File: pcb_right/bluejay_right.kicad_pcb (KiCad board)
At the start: 2 copper layers, 0 parts

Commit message: Begin work on right pcb
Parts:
- added C6: 4.7u, BlueJay footprints:CP_Radial_D4.0mm_P1.50mm, F.Cu at (80.6, 42.8)
- added C7: 100n, BlueJay footprints:C_Disc_D4.3mm_W1.9mm_P5.00mm, F.Cu at (82.0, 87.2)
- added Da1: 1N4148, BlueJay footprints:D_DO-35_SOD27_P5.08mm_Horizontal, F.Cu at (40.7, 127.8)
- added Da2: 1N4148, BlueJay footprints:D_DO-35_SOD27_P5.08mm_Horizontal, F.Cu at (41.2, 134.2)
- added Da3: 1N4148, BlueJay footprints:D_DO-35_SOD27_P5.08mm_Horizontal, F.Cu at (40.9, 139.2)
- added Da4: 1N4148, BlueJay footprints:D_DO-35_SOD27_P5.08mm_Horizontal, F.Cu at (40.4, 145.5)
- added Da5: 1N4148, BlueJay footprints:D_DO-35_SOD27_P5.08mm_Horizontal, F.Cu at (39.7, 152.2)
- added Db1: 1N4148, BlueJay footprints:D_DO-35_SOD27_P5.08mm_Horizontal, F.Cu at (51.9, 128.0)
- added Db2: 1N4148, BlueJay footprints:D_DO-35_SOD27_P5.08mm_Horizontal, F.Cu at (51.7, 133.8)
- added Db3: 1N4148, BlueJay footprints:D_DO-35_SOD27_P5.08mm_Horizontal, F.Cu at (51.7, 138.8)
- added Db4: 1N4148, BlueJay footprints:D_DO-35_SOD27_P5.08mm_Horizontal, F.Cu at (51.9, 145.0)
- added Db5: 1N4148, BlueJay footprints:D_DO-35_SOD27_P5.08mm_Horizontal, F.Cu at (51.7, 152.2)
- added Dc1: 1N4148, BlueJay footprints:D_DO-35_SOD27_P5.08mm_Horizontal, F.Cu at (61.2, 128.0)
- added Dc2: 1N4148, BlueJay footprints:D_DO-35_SOD27_P5.08mm_Horizontal, F.Cu at (61.2, 133.5)
- added Dc3: 1N4148, BlueJay footprints:D_DO-35_SOD27_P5.08mm_Horizontal, F.Cu at (60.9, 138.0)
- added Dc4: 1N4148, BlueJay footprints:D_DO-35_SOD27_P5.08mm_Horizontal, F.Cu at (61.4, 144.5)
- added Dc5: 1N4148, BlueJay footprints:D_DO-35_SOD27_P5.08mm_Horizontal, F.Cu at (61.9, 151.5)
- added Dd1: 1N4148, BlueJay footprints:D_DO-35_SOD27_P5.08mm_Horizontal, F.Cu at (202.2, 11.2)
- added Dd2: 1N4148, BlueJay footprints:D_DO-35_SOD27_P5.08mm_Horizontal, F.Cu at (202.7, 16.2)
- added Dd3: 1N4148, BlueJay footprints:D_DO-35_SOD27_P5.08mm_Horizontal, F.Cu at (202.4, 21.2)
- added Dd4: 1N4148, BlueJay footprints:D_DO-35_SOD27_P5.08mm_Horizontal, F.Cu at (202.4, 25.2)
- added Dd5: 1N4148, BlueJay footprints:D_DO-35_SOD27_P5.08mm_Horizontal, F.Cu at (166.4, 127.5)
- added De1: 1N4148, BlueJay footprints:D_DO-35_SOD27_P5.08mm_Horizontal, F.Cu at (213.2, 11.2)
- added De2: 1N4148, BlueJay footprints:D_DO-35_SOD27_P5.08mm_Horizontal, F.Cu at (213.2, 25.0)
- added De3: 1N4148, BlueJay footprints:D_DO-35_SOD27_P5.08mm_Horizontal, F.Cu at (212.9, 17.5)
- added De4: 1N4148, BlueJay footprints:D_DO-35_SOD27_P5.08mm_Horizontal, F.Cu at (213.2, 21.2)
- added Df2: 1N4148, BlueJay footprints:D_DO-35_SOD27_P5.08mm_Horizontal, F.Cu at (227.9, 47.2)
- added Df3: 1N4148, BlueJay footprints:D_DO-35_SOD27_P5.08mm_Horizontal, F.Cu at (227.7, 51.2)
- added Df4: 1N4148, BlueJay footprints:D_DO-35_SOD27_P5.08mm_Horizontal, F.Cu at (227.9, 55.0)
- added J2: SJ-43514, BlueJay footprints:CUI_SJ-43514, F.Cu at (86.1, 32.5)
- added R5: 2.2k, BlueJay footprints:R_Axial_DIN0204_L3.6mm_D1.6mm_P5.08mm_Horizontal, F.Cu at (85.7, 43.1)
- added R6: 2.2k, BlueJay footprints:R_Axial_DIN0204_L3.6mm_D1.6mm_P5.08mm_Horizontal, F.Cu at (78.6, 37.3)
- added SWa1: KEYSW, BlueJay footprints:SW_MX, F.Cu at (116.7, 47.6)
- added SWa2: KEYSW, BlueJay footprints:SW_MX, F.Cu at (116.7, 66.7)
- added SWa3: KEYSW, BlueJay footprints:SW_MX, F.Cu at (116.7, 85.7)
- added SWa4: KEYSW, BlueJay footprints:SW_MX, F.Cu at (116.7, 104.8)
- added SWa5: KEYSW, BlueJay footprints:SW_MX, F.Cu at (87.5, 152.9)
- added SWb1: KEYSW, BlueJay footprints:SW_MX, F.Cu at (135.7, 45.2)
- added SWb2: KEYSW, BlueJay footprints:SW_MX, F.Cu at (135.7, 64.3)
- added SWb3: KEYSW, BlueJay footprints:SW_MX, F.Cu at (135.7, 83.3)
- added SWb4: KEYSW, BlueJay footprints:SW_MX, F.Cu at (135.7, 102.4)
- added SWb5: KEYSW, BlueJay footprints:SW_MX, F.Cu at (104.8, 140.5)
- added SWc1: KEYSW, BlueJay footprints:SW_MX, F.Cu at (154.8, 38.1)
- added SWc2: KEYSW, BlueJay footprints:SW_MX, F.Cu at (154.8, 57.1)
- added SWc3: KEYSW, BlueJay footprints:SW_MX, F.Cu at (154.8, 76.2)
- added SWc4: KEYSW, BlueJay footprints:SW_MX, F.Cu at (154.8, 95.2)
- added SWc5: KEYSW, BlueJay footprints:SW_MX, F.Cu at (123.8, 133.3)
- added SWd1: KEYSW, BlueJay footprints:SW_MX, F.Cu at (173.8, 45.2)
- added SWd2: KEYSW, BlueJay footprints:SW_MX, F.Cu at (173.8, 64.3)
- added SWd3: KEYSW, BlueJay footprints:SW_MX, F.Cu at (173.8, 83.3)
- added SWd4: KEYSW, BlueJay footprints:SW_MX, F.Cu at (173.8, 102.4)
- added SWd5: KEYSW, BlueJay footprints:SW_MX, F.Cu at (145.3, 128.6)
- added SWe1: KEYSW, BlueJay footprints:SW_MX, F.Cu at (192.9, 52.4)
- added SWe2: KEYSW, BlueJay footprints:SW_MX, F.Cu at (192.9, 71.4)
- added SWe3: KEYSW, BlueJay footprints:SW_MX, F.Cu at (192.9, 90.5)
- added SWe4: KEYSW, BlueJay footprints:SW_MX, F.Cu at (192.9, 109.5)
- added SWf2: KEYSW, BlueJay footprints:SW_MX, F.Cu at (211.9, 71.4)
- added SWf3: KEYSW, BlueJay footprints:SW_MX, F.Cu at (211.9, 90.5)
- added SWf4: KEYSW, BlueJay footprints:SW_MX, F.Cu at (211.9, 109.5)
- added U2: MCP23017, Package_DIP_AKL:DIP-28_W7.62mm_Socket, F.Cu at (84.9, 68.1)
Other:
- board outline added: 147 x 140.5 mm

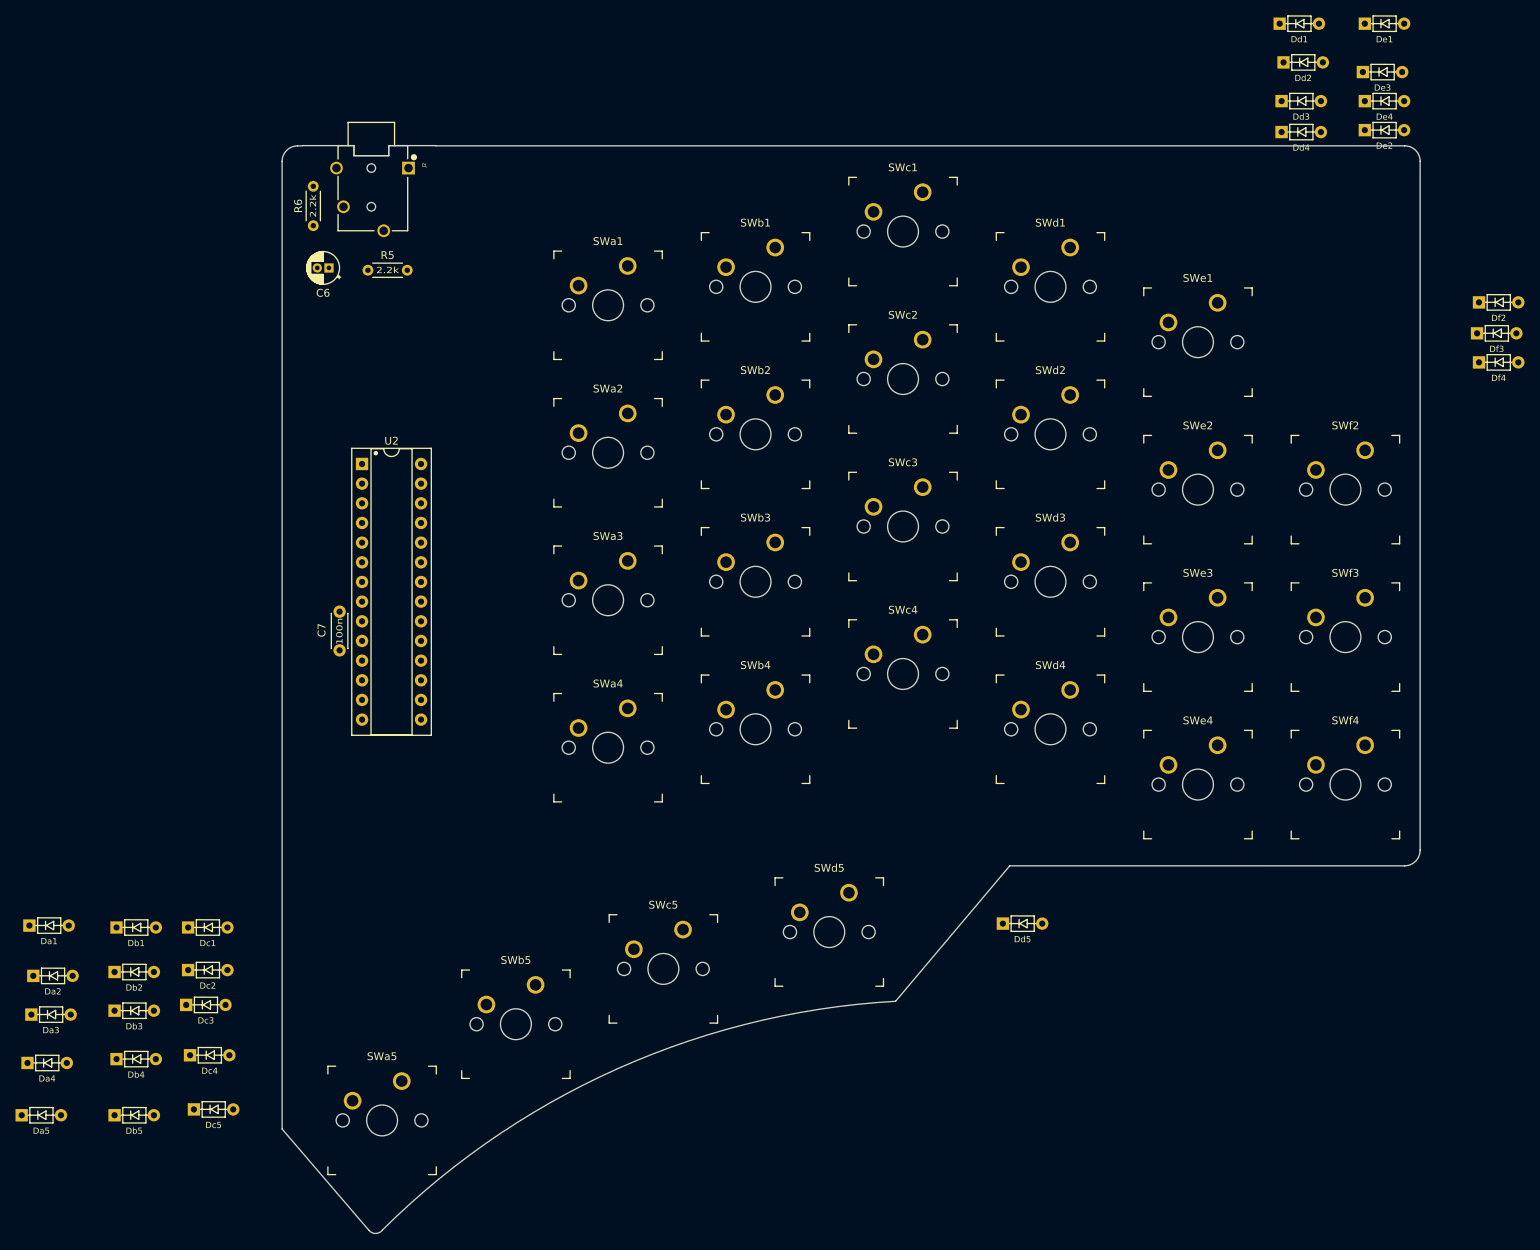
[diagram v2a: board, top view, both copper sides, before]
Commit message: Routing of right PCB
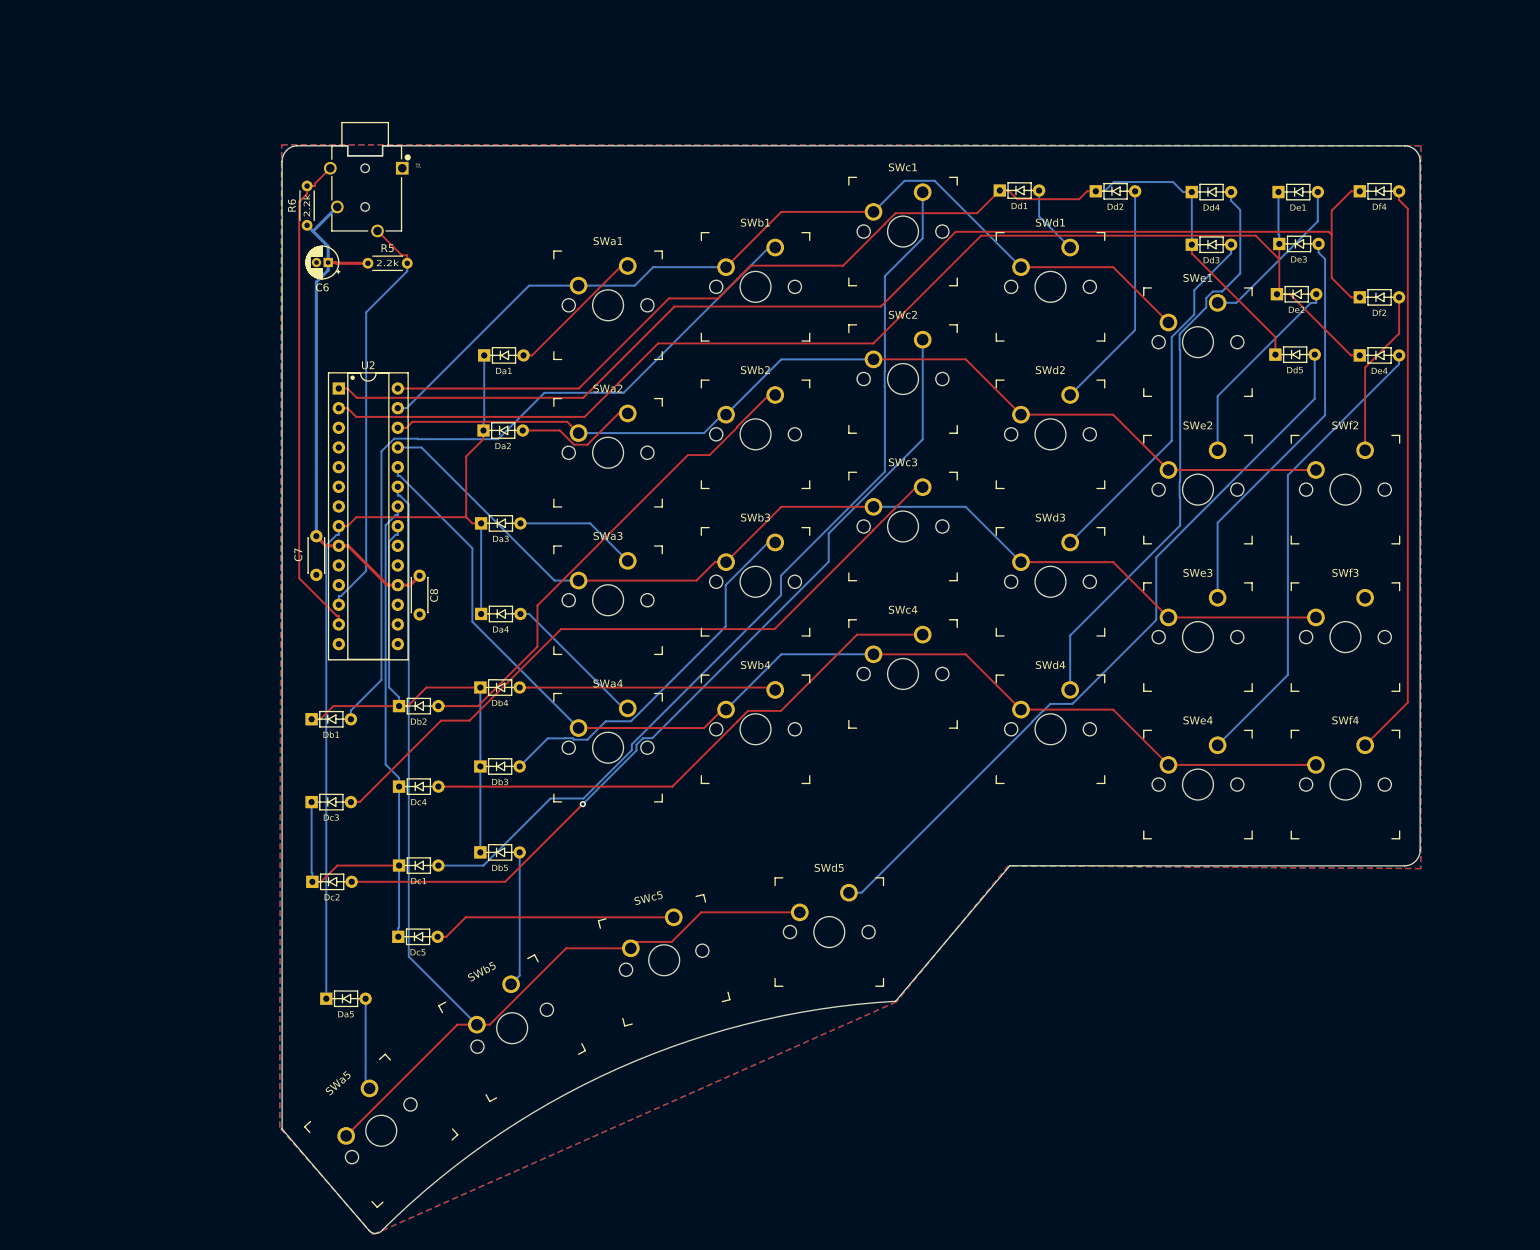
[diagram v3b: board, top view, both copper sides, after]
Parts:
- removed Df3: 1N4148, BlueJay footprints:D_DO-35_SOD27_P5.08mm_Horizontal
- added C8: 100n, BlueJay footprints:C_Disc_D4.3mm_W1.9mm_P5.00mm, F.Cu at (92.3, 82.6)
- moved Da1 94.2 mm to (99.4, 54.1)
- moved Da2 91.3 mm to (99.3, 63.8)
- moved Da3 86.0 mm to (99.0, 75.8)
- moved Da4 82.4 mm to (99.0, 87.5)
- moved Dd5 81.5 mm to (201.6, 54.0)
- moved Db4 67.2 mm to (98.9, 97.0)
- moved Db5 58.2 mm to (98.9, 118.3)
- moved Db3 56.8 mm to (98.9, 107.2)
- moved Db2 50.3 mm to (88.4, 99.4)
- moved Dc4 44.0 mm to (88.4, 109.8)
- moved Da5 42.1 mm to (79.0, 137.2)
- moved Dd1 42.1 mm to (166.0, 32.8)
- moved Db1 36.9 mm to (77.1, 101.1)
- moved Dc5 34.6 mm to (88.3, 129.2)
- moved De4 32.9 mm to (212.5, 54.1)
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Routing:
- net /colE: track 0.00 -> 160.1 mm
- net /colF: track 0.00 -> 155.8 mm
- net /row4: track 0.00 -> 148.7 mm
- net /row5: track 0.00 -> 144.4 mm
- net /colD: track 0.00 -> 140.6 mm
- net /row3: track 0.00 -> 135.6 mm
- net /row2: track 0.00 -> 129.4 mm
- net /row1: track 0.00 -> 119.3 mm
- net Net-(Dc1-Pad2): track 0.00 -> 118.8 mm
- net /colA: track 0.00 -> 114.6 mm
- net Net-(Dc2-Pad2): track 0.00 -> 112.9 mm, vias 0 -> 1
- net Net-(Db1-Pad2): track 0.00 -> 98.1 mm
- net Net-(Dd5-Pad2): track 0.00 -> 97.1 mm
- net Net-(Dc3-Pad2): track 0.00 -> 90.7 mm
- net /colC: track 0.00 -> 79.6 mm
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- added copper zone on B.Cu, net GND
- added copper zone on F.Cu, net GND
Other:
- outline, holes or cut-outs redrawn

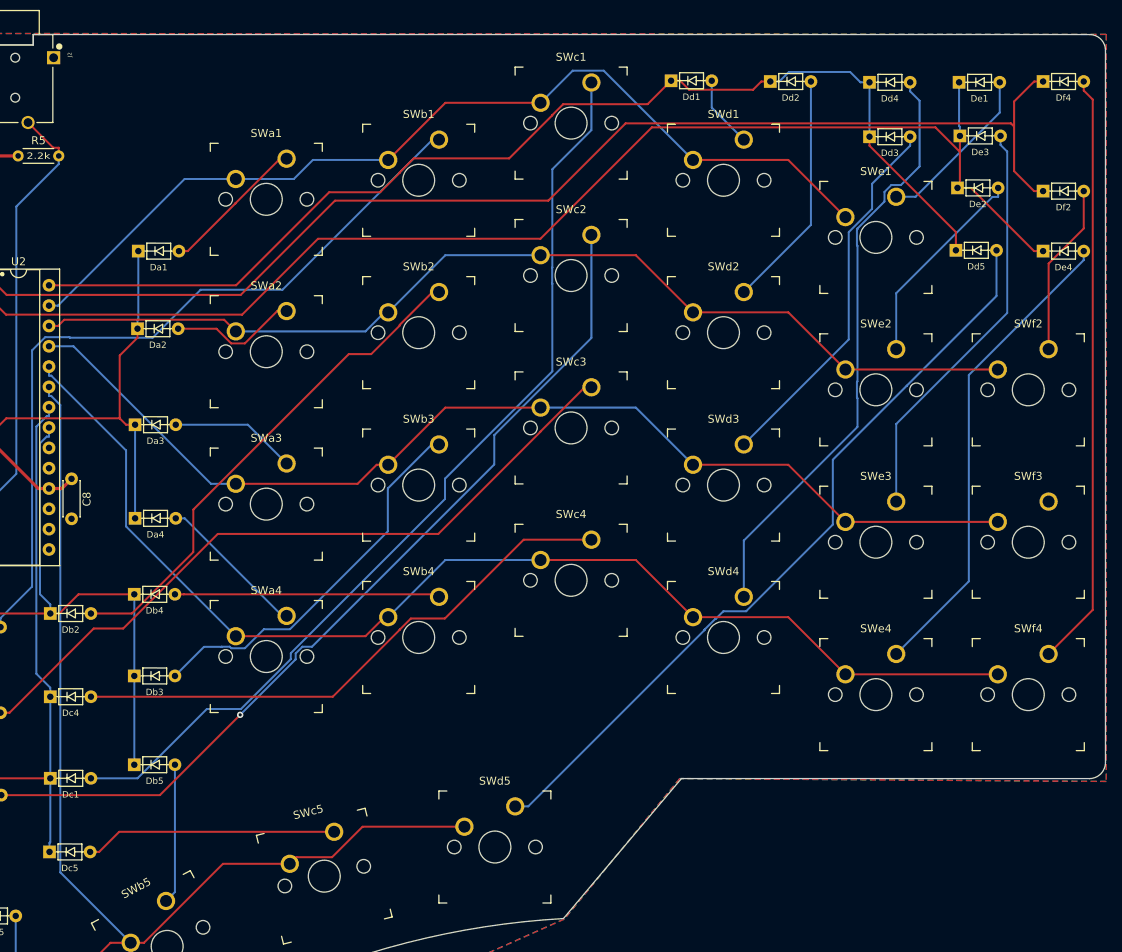
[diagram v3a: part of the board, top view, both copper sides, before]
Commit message: Fine tune placement of switches - right hand
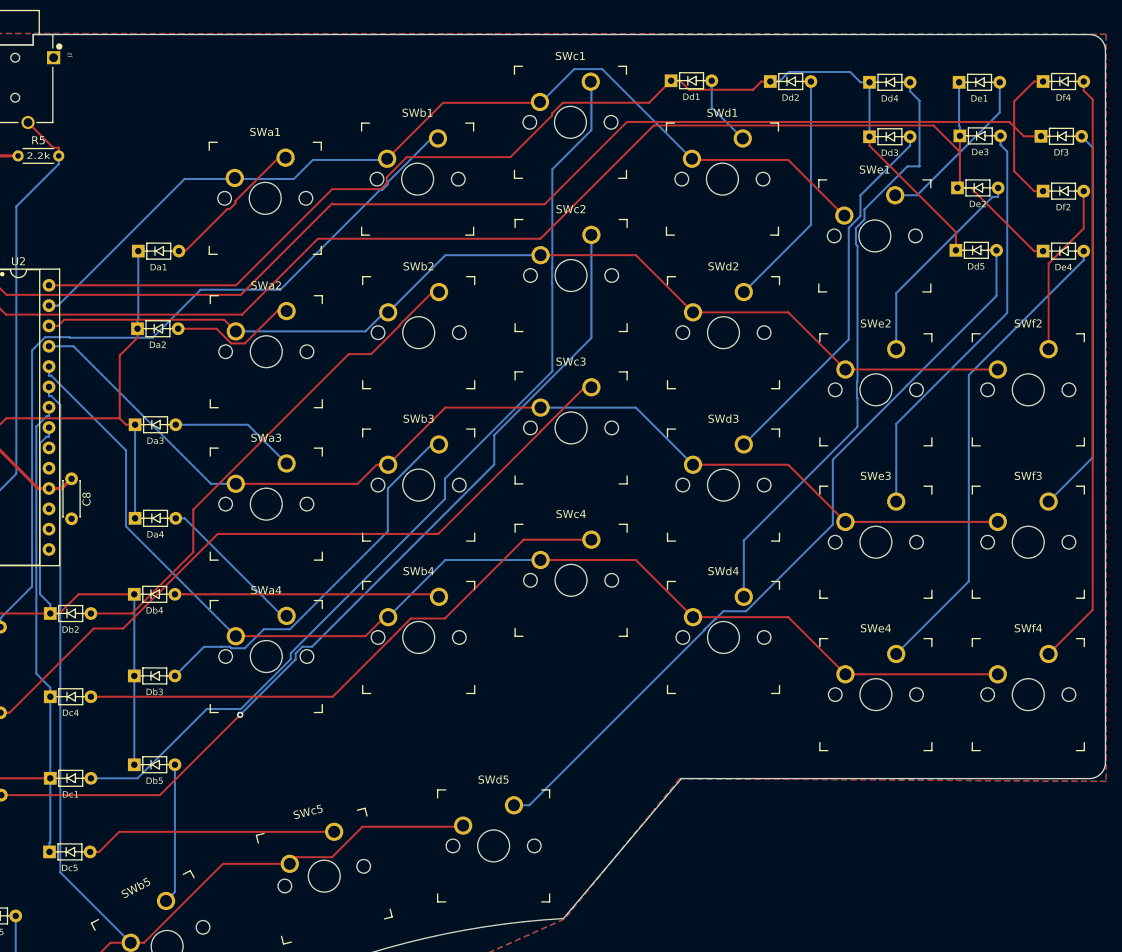
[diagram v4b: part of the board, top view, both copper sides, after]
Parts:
- added Df3: 1N4148, BlueJay footprints:D_DO-35_SOD27_P5.08mm_Horizontal, F.Cu at (212.2, 39.8)
- moved SWe1 0.23 mm to (192.8, 52.2)
- moved SWd5 0.21 mm to (145.1, 128.4)
- moved SWb1 0.19 mm to (135.6, 45.1)
- moved SWd1 0.19 mm to (173.7, 45.1)
- moved SWa1 0.18 mm to (116.5, 47.5)
- moved SWc1 0.13 mm to (154.7, 38.0)
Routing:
- net Net-(Df3-Pad2): track 0.00 -> 48.5 mm
- net /colF: track 155.8 -> 159.7 mm
